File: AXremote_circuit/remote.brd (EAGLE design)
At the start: 240 x 49 mm, 64 parts, among them Q1 16MHz, U1 AX8052F143HS

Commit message: Routed rev4, all SMD.
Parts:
- removed U$1: CR2032, sam_eagle_parts:CRC2032HOLDER
- removed U$3: APERTURE_LOGO, sam_eagle_parts:APERTURE_LOGO
- added BATTERY: BATTERYSMD, sam:CR2032-SMD
- added L7: (no value), SparkFun-Passives:NPI75C
- added U$4: (no value), sam:APERTURE_LOGO
- R4: value (none) -> 10k
- moved S34 319.0 mm to (232.8, 12.2), turned to 180 degrees
- moved S31 303.0 mm to (220.5, 12.2), turned to 180 degrees
- moved S32 301.7 mm to (220.5, 24.5), turned to 180 degrees
- moved S28 287.0 mm to (208.2, 12.2), turned to 180 degrees
- moved S29 285.5 mm to (208.2, 24.5), turned to 180 degrees
- moved S30 284.6 mm to (208.2, 36.8), turned to 180 degrees
- moved S25 265.5 mm to (189.9, 12.2), turned to 180 degrees
- moved S26 263.8 mm to (189.9, 24.5), turned to 180 degrees
- moved S27 262.8 mm to (189.9, 36.8), turned to 180 degrees
- moved S22 244.1 mm to (171.5, 12.2), turned to 180 degrees
- moved S23 242.1 mm to (171.5, 24.5), turned to 180 degrees
- moved S24 240.9 mm to (171.5, 36.8), turned to 180 degrees
- moved S19 228.6 mm to (159.2, 12.2), turned to 180 degrees
- moved S20 226.2 mm to (159.2, 24.5), turned to 180 degrees
- moved S21 224.7 mm to (159.2, 36.8), turned to 180 degrees
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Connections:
- removed net ROW10: S16.P3
- removed net ROW11: S22.P3
- removed net ROW12: S28.P3
- removed net ROW13: S34.P3
- removed net ROW9: S10.P3
- new net N$18: BATTERY.PLUS, L7.1
- net COL0: now also S13.P1, S13.P2, S19.P1, S19.P2, S25.P1, S25.P2, S31.P1, S31.P2, S7.P1, S7.P2
- net COL1: now also S14.P1, S14.P2, S20.P1, S20.P2, S26.P1, S26.P2, S32.P1, S32.P2, S8.P1, S8.P2
- net COL2: now also S15.P1, S15.P2, S21.P1, S21.P2, S27.P1, S27.P2, S9.P1, S9.P2
- net COL3: now also S10.P1, S10.P2, S16.P1, S16.P2, S22.P1, S22.P2, S28.P1, S28.P2, S34.P1, S34.P2
- net COL4: now also S11.P1, S11.P2, S17.P1, S17.P2, S23.P1, S23.P2, S29.P1, S29.P2
- net COL5: now also S12.P1, S12.P2, S18.P1, S18.P2, S24.P1, S24.P2, S30.P1, S30.P2
- net GND: now also BATTERY.MINUS; no longer U$1.P$MINUS
- net ROW1: now also S10.P3, S10.P4, S11.P3, S11.P4, S12.P3, S12.P4, S7.P3, S7.P4, S8.P3, S8.P4, S9.P3, S9.P4
- net ROW2: now also S13.P3, S13.P4, S14.P3, S14.P4, S15.P3, S15.P4, S16.P3, S16.P4, S17.P3, S17.P4, S18.P3, S18.P4
- net ROW3: now also S19.P3, S19.P4, S20.P3, S20.P4, S21.P3, S21.P4, S22.P3, S22.P4, S23.P3, S23.P4, S24.P3, S24.P4
- net ROW4: now also S25.P3, S25.P4, S26.P3, S26.P4, S27.P3, S27.P4, S28.P3, S28.P4, S29.P3, S29.P4, S30.P3, S30.P4
- net ROW5: now also S31.P3, S31.P4, S32.P3, S32.P4, S34.P3, S34.P4
- net VCC: now also L7.2; no longer U$1.P$PLUS1, U$1.P$PLUS2
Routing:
- net COL0: track 0.00 -> 277.4 mm, vias 0 -> 7
- net COL1: track 0.00 -> 273.6 mm, vias 0 -> 7
- net COL3: track 0.00 -> 263.3 mm, vias 0 -> 6
- net ROW4: track 0.00 -> 245.4 mm, vias 0 -> 2
- net COL5: track 0.00 -> 239.1 mm, vias 0 -> 6
- net ROW5: track 0.00 -> 232.9 mm, vias 0 -> 2
- net COL4: track 0.00 -> 231.2 mm, vias 0 -> 6
- net ROW0: track 0.00 -> 230.8 mm, vias 0 -> 2
- net COL2: track 0.00 -> 227.7 mm, vias 0 -> 6
- net ROW3: track 0.00 -> 212.8 mm
- net ROW2: track 0.00 -> 186.2 mm
- net ROW1: track 0.00 -> 146.0 mm
- net GND: track 50.7 -> 20.4 mm, vias 3 -> 68
- net N$18: track 0.00 -> 23.3 mm, vias 0 -> 2
- net VCC: track 76.1 -> 61.7 mm, vias 4 -> 2
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- added copper zone on layer 16, net GND
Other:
- board text added: "Samuel Bryner, 2014, rev 4"
- board text removed: "Samuel Bryner, 2014, rev 3"

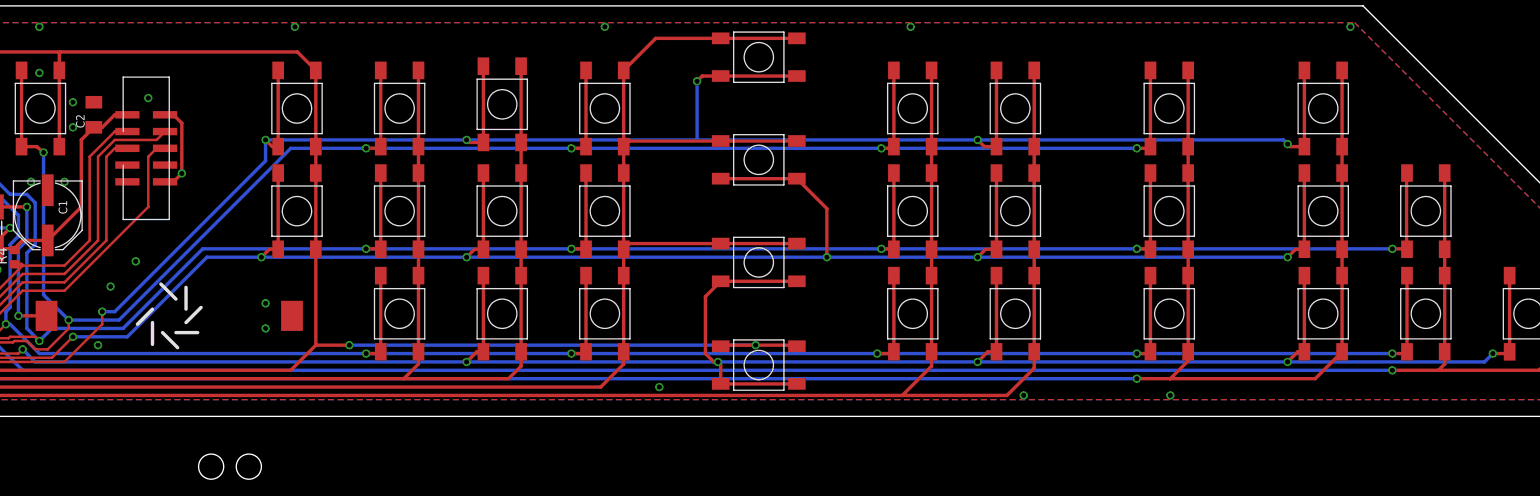
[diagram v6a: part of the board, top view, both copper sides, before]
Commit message: Add labels, holes and decoration.
Should be ready for production now.
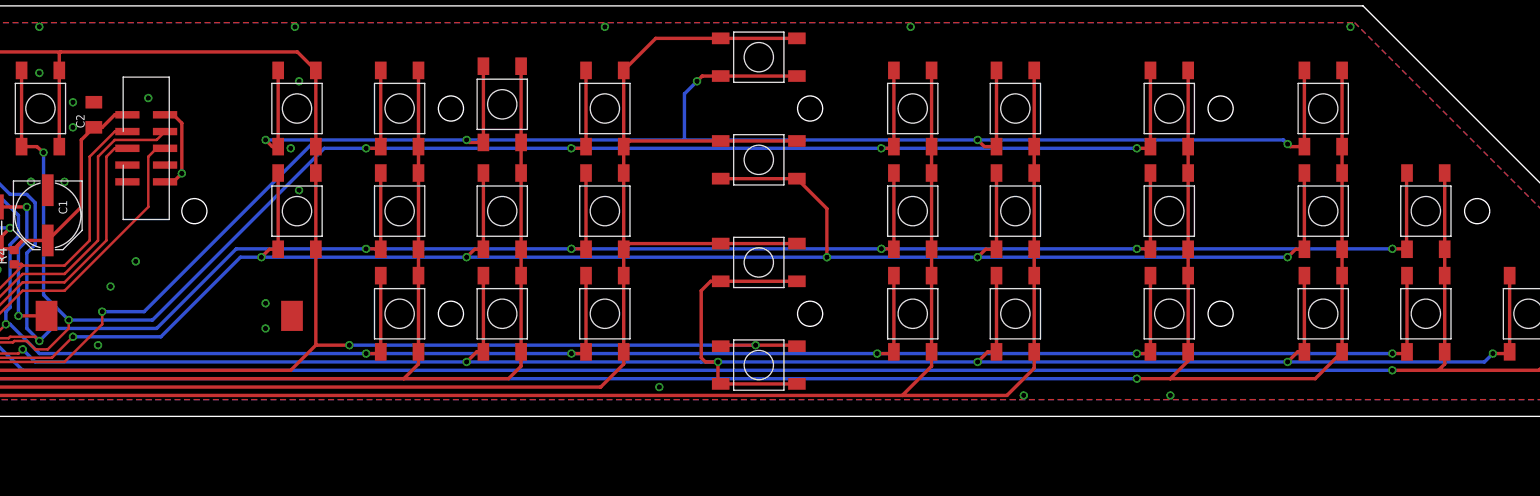
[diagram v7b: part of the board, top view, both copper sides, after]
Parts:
- added U$1, U$10, U$11, U$12: (no value), sam_icons:ARROW
- added U$13, U$14: (no value), sam_icons:ARROW_DOUBLE
- added U$15: (no value), sam_icons:ARROW_BACK
- added U$16: (no value), sam_icons:PLAY_PAUSE
- added U$17, U$18: (no value), sam_icons:FAST_FORWARD
- added U$19, U$20: (no value), sam_icons:FAST_FORWARD_NEXT
- added U$21, U$22, U$23: (no value), sam_icons:PLUS
- added U$24, U$25, U$26: (no value), sam_icons:MINUS
- added U$27: (no value), sam_icons:ARROW_ROT_RIGHT
- added U$3: pc, sam_icons:POWER_TEXT
- added U$5: TV, sam_icons:POWER_TEXT
- added U$6: AUDIO, sam_icons:POWER_TEXT
- added U$7: (no value), sam_icons:HOME
- added U$9: (no value), sam_icons:STOP
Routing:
- net COL5: track 239.1 -> 244.2 mm
- net COL3: track 263.3 -> 265.5 mm
- net GND: vias 68 -> 71
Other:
- board text added: "1:1"
- board text added: "ASPECT R."
- board text added: "CHANNEL"
- board text added: "CTX-MENU"
- board text added: "INFO"
- board text added: "MUTE"
- board text added: "NEXT"
- board text added: "OK"
- board text added: "SUBTITLE"
- board text added: "Samuel Bryner (2014, rev 4)"
- board text added: "TV-PROG"
- board text added: "Use raster of 6.125mm for buttons, labels and holes."
- board text added: "VOL"
- board text added: "ZOOM"
- board text removed: "Samuel Bryner, 2014, rev 4"
